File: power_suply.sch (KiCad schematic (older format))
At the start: 25 parts

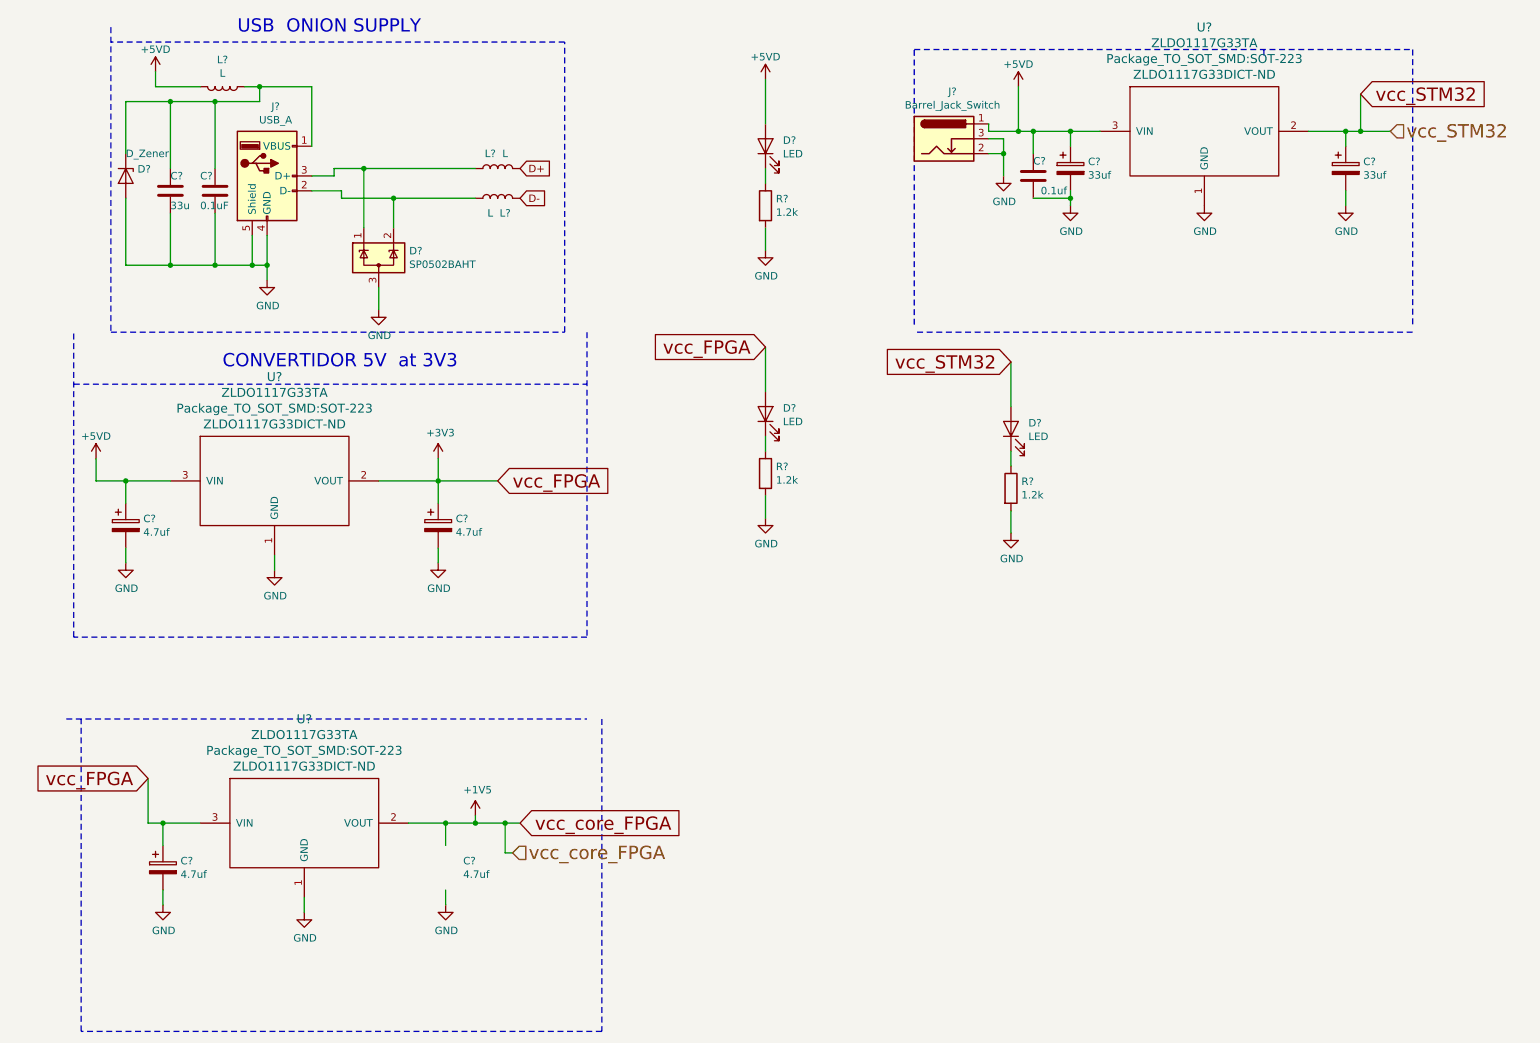
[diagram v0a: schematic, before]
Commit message: asignacion pines de control
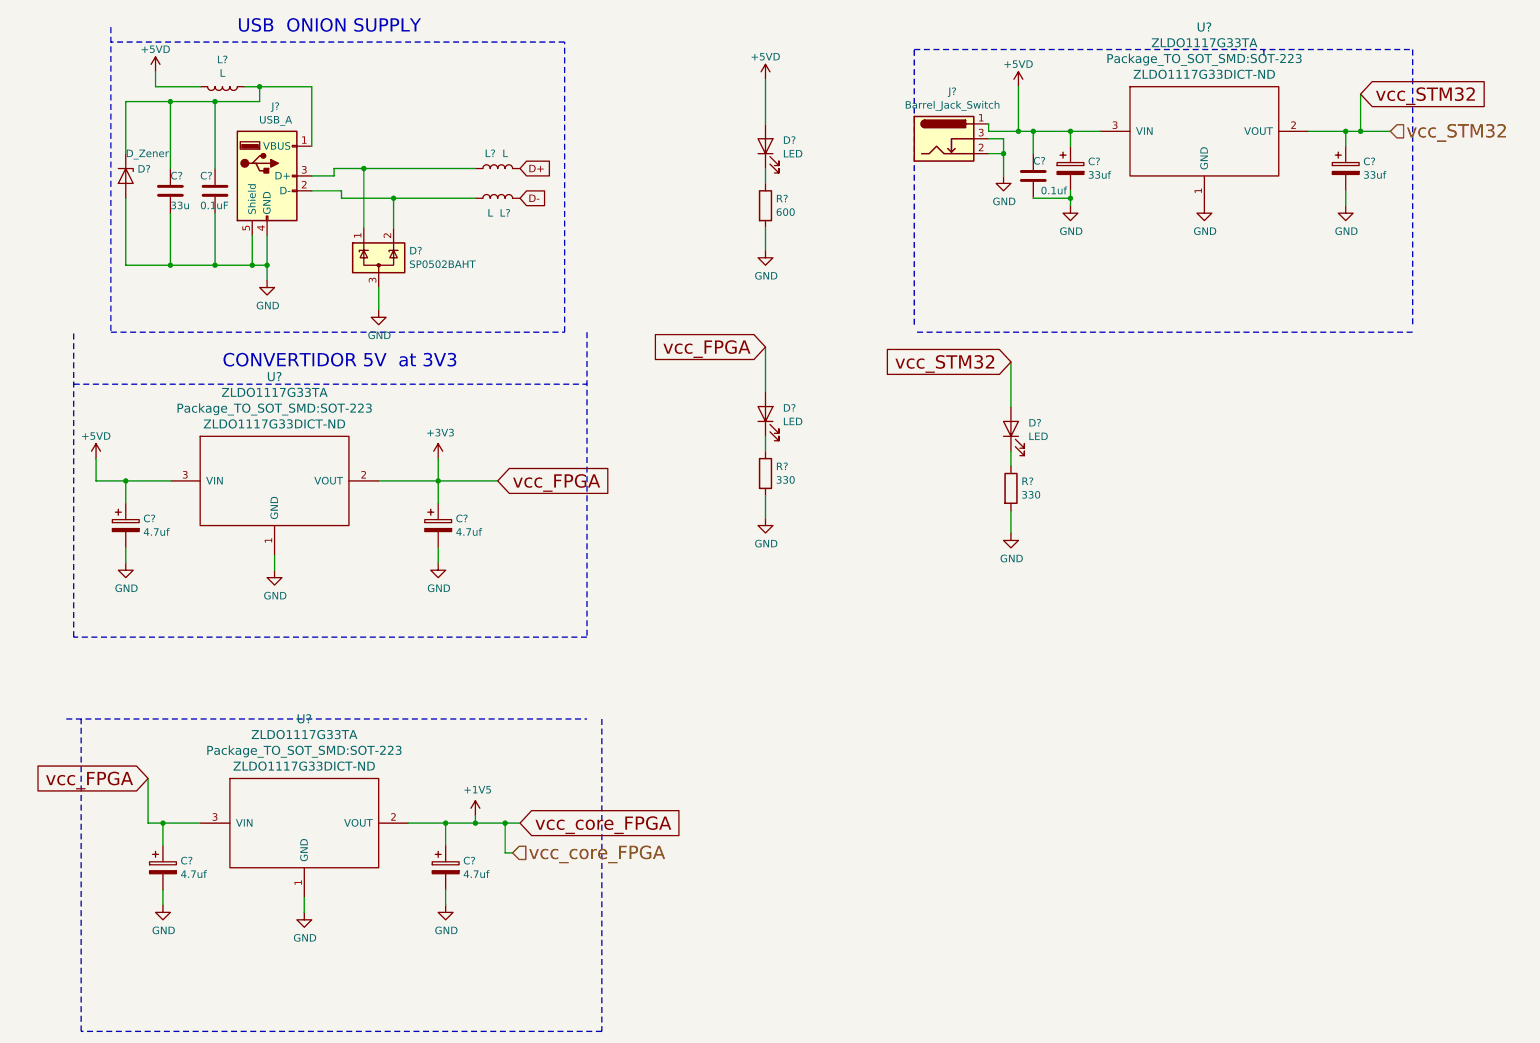
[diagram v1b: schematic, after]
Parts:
- removed D? (x2): LED, symbol BAT2032:LED
- added D? (x2): LED, LED_SMD:LED_0603_1608Metric, symbol BAT2032:LED
- D?: footprint (none) -> LED_SMD:LED_0603_1608Metric; digikey (none) -> 160-1436-1-ND rojo
- R?: value 1.2k -> 600
- R? (x2): value 1.2k -> 330
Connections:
- net +1V5: now also C?.1
- net +3V3: now also D?.2 (A)
- net GND: now also C?.2
- net vcc_STM32: now also D?.2 (A)
- net at R?.1: now also D?.1 (K) (x2)
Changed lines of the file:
@@
 $Descr A4 11693 8268
 encoding utf-8
-Sheet 2 5
+Sheet 2 6
 Title ""
 Date ""
@@
 $Comp
 L Device:CP C?
-U 0 0 5CD685F9
+U 1 1 5CD685F9
 P 3800 6500
 F 0 "C?" H 3918 6546 50  0000 L CNN
@@
 F 2 "" H 3838 6350 50  0001 C CNN
 F 3 "~" H 3800 6500 50  0001 C CNN
-	0    3800 6500
+	1    3800 6500
 	1    0    0    -1
 $EndComp
@@
 F 0 "D?" V 5989 1533 50  0000 R CNN
 F 1 "LED" V 5898 1533 50  0000 R CNN
-F 2 "" H 5950 1650 50  0001 C CNN
-F 3 "~" H 5950 1650 50  0001 C CNN
+F 2 "LED_SMD:LED_0603_1608Metric" H 5950 1650 50  0001 C CNN
+F 3 "http://optoelectronics.liteon.com/upload/download/DS-22-99-0151/LTST-C190KRKT.pdf" H 5950 1650 50  0001 C CNN
+F 4 "160-1436-1-ND     rojo" V 5950 1650 50  0001 C CNN "digikey"
 	1    5950 1650
 	0    -1   -1   0
@@
 P 5950 2050
 F 0 "R?" H 6020 2096 50  0000 L CNN
-F 1 "1.2k" H 6020 2005 50  0000 L CNN
+F 1 "600" H 6020 2005 50  0000 L CNN
 F 2 "Resistor_SMD:R_0603_1608Metric_Pad1.05x0.95mm_HandSolder" V 5880 2050 50  0001 C CNN
 F 3 "~" H 5950 2050 50  0001 C CNN
+F 4 "" H 5950 2050 50  0001 C CNN "Digikey"
 	1    5950 2050
 	1    0    0    -1
@@
 	5950 3000 5950 3300
 $Comp
-L BAT2032:LED D?
-U 1 1 5D5F584F
-P 5950 3450
-F 0 "D?" V 5989 3333 50  0000 R CNN
-F 1 "LED" V 5898 3333 50  0000 R CNN
-F 2 "" H 5950 3450 50  0001 C CNN
-F 3 "~" H 5950 3450 50  0001 C CNN
-	1    5950 3450
-	0    -1   -1   0
-$EndComp
-$Comp
 L BAT2032:R R?
 U 1 1 5D5F5855
 P 5950 3850
 F 0 "R?" H 6020 3896 50  0000 L CNN
-F 1 "1.2k" H 6020 3805 50  0000 L CNN
+F 1 "330" H 6020 3805 50  0000 L CNN
 F 2 "Resistor_SMD:R_0603_1608Metric_Pad1.05x0.95mm_HandSolder" V 5880 3850 50  0001 C CNN
 F 3 "~" H 5950 3850 50  0001 C CNN
@@
 	7600 3100 7600 3400
 $Comp
-L BAT2032:LED D?
-U 1 1 5D60A5BF
-P 7600 3550
-F 0 "D?" V 7639 3433 50  0000 R CNN
-F 1 "LED" V 7548 3433 50  0000 R CNN
-F 2 "" H 7600 3550 50  0001 C CNN
-F 3 "~" H 7600 3550 50  0001 C CNN
-	1    7600 3550
-	0    -1   -1   0
-$EndComp
-$Comp
 L BAT2032:R R?
 U 1 1 5D60A5C5
 P 7600 3950
 F 0 "R?" H 7670 3996 50  0000 L CNN
-F 1 "1.2k" H 7670 3905 50  0000 L CNN
+F 1 "330" H 7670 3905 50  0000 L CNN
 F 2 "Resistor_SMD:R_0603_1608Metric_Pad1.05x0.95mm_HandSolder" V 7530 3950 50  0001 C CNN
 F 3 "~" H 7600 3950 50  0001 C CNN
@@
 Text GLabel 7600 3100 0    89   Input ~ 0
 vcc_STM32
+$Comp
+L BAT2032:LED D?
+U 1 1 5D364419
+P 5950 3450
+F 0 "D?" V 5989 3333 50  0000 R CNN
+F 1 "LED" V 5898 3333 50  0000 R CNN
+F 2 "LED_SMD:LED_0603_1608Metric" H 5950 3450 50  0001 C CNN
+F 3 "~https://www.rohm.com/datasheet/SML-D12U1W" H 5950 3450 50  0001 C CNN
+F 4 "	846-1176-1-ND  Verde" V 5950 3450 50  0001 C CNN "digikey"
+	1    5950 3450
+	0    -1   -1   0
+$EndComp
+$Comp
+L BAT2032:LED D?
+U 1 1 5D366F3A
+P 7600 3550
+F 0 "D?" V 7639 3433 50  0000 R CNN
+F 1 "LED" V 7548 3433 50  0000 R CNN
+F 2 "LED_SMD:LED_0603_1608Metric" H 7600 3550 50  0001 C CNN
+F 3 "http://optoelectronics.liteon.com/upload/download/DS22-2010-0025/LTST-C194TBKT.PDF" H 7600 3550 50  0001 C CNN
+F 4 "160-1837-1-ND azul" V 7600 3550 50  0001 C CNN "digikey"
+	1    7600 3550
+	0    -1   -1   0
+$EndComp
 $EndSCHEMATC

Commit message: asignacion pines de control
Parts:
- gave numbers to parts that had none: 25

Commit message: retoque casi finales
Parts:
- added R13: 100, Resistor_SMD:R_0603_1608Metric_Pad1.05x0.95mm_HandSolder, symbol BAT2032:R
- C2, C3, C6: footprint (none) -> Capacitor_SMD:C_0603_1608Metric_Pad1.05x0.95mm_HandSolder
- D3, D4, D5: footprint LED_SMD:LED_0603_1608Metric -> LED_SMD:LED_0603_1608Metric_Pad1.05x0.95mm_HandSolder
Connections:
- wire segments 89 -> 94
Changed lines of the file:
@@
 F 0 "C3" H 1950 2050 50  0000 L CNN
 F 1 "33u" H 1950 1850 50  0000 L CNN
-F 2 "" H 1988 1800 50  0001 C CNN
+F 2 "Capacitor_SMD:C_0603_1608Metric_Pad1.05x0.95mm_HandSolder" H 1988 1800 50  0001 C CNN
 F 3 "~" H 1950 1950 50  0001 C CNN
 	1    1950 1950
@@
 F 0 "C2" H 2018 6546 50  0000 L CNN
 F 1 "4.7uf" H 2018 6455 50  0000 L CNN
-F 2 "" H 1938 6350 50  0001 C CNN
+F 2 "Capacitor_SMD:C_0603_1608Metric_Pad1.05x0.95mm_HandSolder" H 1938 6350 50  0001 C CNN
 F 3 "~" H 1900 6500 50  0001 C CNN
 	1    1900 6500
@@
 F 0 "C6" H 3918 6546 50  0000 L CNN
 F 1 "4.7uf" H 3918 6455 50  0000 L CNN
-F 2 "" H 3838 6350 50  0001 C CNN
+F 2 "Capacitor_SMD:C_0603_1608Metric_Pad1.05x0.95mm_HandSolder" H 3838 6350 50  0001 C CNN
 F 3 "~" H 3800 6500 50  0001 C CNN
 	1    3800 6500
@@
 vcc_FPGA
 Wire Wire Line
-	2150 6200 1900 6200
-Wire Wire Line
 	1800 6200 1800 5900
 Wire Wire Line
@@
 	1    0    0    -1
 $EndComp
-Wire Wire Line
-	3550 6200 3800 6200
 Wire Wire Line
 	4000 6200 4000 6150
@@
 $Comp
 L pcb_embedded_systems-cache:ZLDO1117G33TA U1
-U 1 1 5CDB7BFB
+U 0 0 5CDB7BFB
 P 2650 3900
 F 0 "U1" H 2650 4599 60  0000 C CNN
 F 1 "ZLDO1117G33TA" H 2650 4493 60  0000 C CNN
-F 2 "Package_TO_SOT_SMD:SOT-223" H 2650 4387 60  0000 C CNN
-F 3 "ZLDO1117G33DICT-ND" H 2650 4281 60  0000 C CNN
+F 2 "Package_TO_SOT_SMD:SOT-223" H 2650 4387 60  0001 C CNN
+F 3 "ZLDO1117G33DICT-ND" H 2650 4281 60  0001 C CNN
 F 4 "https://www.diodes.com/assets/Datasheets/ZLDO1117.pdf" H 2650 3900 50  0001 C CNN "digikey"
-	1    2650 3900
+	0    2650 3900
 	1    0    0    -1
 $EndComp
 $Comp
 L pcb_embedded_systems-cache:ZLDO1117G33TA U2
-U 1 1 5CE0B1BC
+U 0 0 5CE0B1BC
 P 2850 6200
 F 0 "U2" H 2850 6899 60  0000 C CNN
 F 1 "ZLDO1117G33TA" H 2850 6793 60  0000 C CNN
-F 2 "Package_TO_SOT_SMD:SOT-223" H 2850 6687 60  0000 C CNN
-F 3 "ZLDO1117G33DICT-ND" H 2850 6581 60  0000 C CNN
+F 2 "Package_TO_SOT_SMD:SOT-223" H 2850 6687 60  0001 C CNN
+F 3 "ZLDO1117G33DICT-ND" H 2850 6581 60  0001 C CNN
 F 4 "https://www.diodes.com/assets/Datasheets/ZLDO1117.pdf" H 2850 6200 50  0001 C CNN "digikey"
-	1    2850 6200
+	0    2850 6200
 	1    0    0    -1
 $EndComp
 $Comp
 L pcb_embedded_systems-cache:ZLDO1117G33TA U3
-U 1 1 5CE35DA7
+U 0 0 5CE35DA7
 P 8900 1550
 F 0 "U3" H 8900 2249 60  0000 C CNN
 F 1 "ZLDO1117G33TA" H 8900 2143 60  0000 C CNN
-F 2 "Package_TO_SOT_SMD:SOT-223" H 8900 2037 60  0000 C CNN
-F 3 "ZLDO1117G33DICT-ND" H 8900 1931 60  0000 C CNN
+F 2 "Package_TO_SOT_SMD:SOT-223" H 8900 2037 60  0001 C CNN
+F 3 "ZLDO1117G33DICT-ND" H 8900 1931 60  0001 C CNN
 F 4 "https://www.diodes.com/assets/Datasheets/ZLDO1117.pdf" H 8900 1550 50  0001 C CNN "digikey"
-	1    8900 1550
+	0    8900 1550
 	1    0    0    -1
 $EndComp
@@
 F 0 "D3" V 5989 1533 50  0000 R CNN
 F 1 "LED" V 5898 1533 50  0000 R CNN
-F 2 "LED_SMD:LED_0603_1608Metric" H 5950 1650 50  0001 C CNN
+F 2 "LED_SMD:LED_0603_1608Metric_Pad1.05x0.95mm_HandSolder" H 5950 1650 50  0001 C CNN
 F 3 "http://optoelectronics.liteon.com/upload/download/DS-22-99-0151/LTST-C190KRKT.pdf" H 5950 1650 50  0001 C CNN
 F 4 "160-1436-1-ND     rojo" V 5950 1650 50  0001 C CNN "digikey"
@@
 F 0 "D4" V 5989 3333 50  0000 R CNN
 F 1 "LED" V 5898 3333 50  0000 R CNN
-F 2 "LED_SMD:LED_0603_1608Metric" H 5950 3450 50  0001 C CNN
+F 2 "LED_SMD:LED_0603_1608Metric_Pad1.05x0.95mm_HandSolder" H 5950 3450 50  0001 C CNN
 F 3 "~https://www.rohm.com/datasheet/SML-D12U1W" H 5950 3450 50  0001 C CNN
 F 4 "	846-1176-1-ND  Verde" V 5950 3450 50  0001 C CNN "digikey"
@@
 F 0 "D5" V 7639 3433 50  0000 R CNN
 F 1 "LED" V 7548 3433 50  0000 R CNN
-F 2 "LED_SMD:LED_0603_1608Metric" H 7600 3550 50  0001 C CNN
+F 2 "LED_SMD:LED_0603_1608Metric_Pad1.05x0.95mm_HandSolder" H 7600 3550 50  0001 C CNN
 F 3 "http://optoelectronics.liteon.com/upload/download/DS22-2010-0025/LTST-C194TBKT.PDF" H 7600 3550 50  0001 C CNN
 F 4 "160-1837-1-ND azul" V 7600 3550 50  0001 C CNN "digikey"
@@
 	0    -1   -1   0
 $EndComp
+$Comp
+L BAT2032:R R13
+U 1 1 5DF0C6DE
+P 2850 7250
+F 0 "R13" V 2750 7250 50  0000 C CNN
+F 1 "100" V 2850 7250 50  0000 C CNN
+F 2 "Resistor_SMD:R_0603_1608Metric_Pad1.05x0.95mm_HandSolder" V 2780 7250 50  0001 C CNN
+F 3 "~" H 2850 7250 50  0001 C CNN
+	1    2850 7250
+	0    1    1    0
+$EndComp
+Wire Wire Line
+	2150 6200 1900 6200
+Wire Wire Line
+	3550 6200 3600 6200
+Wire Wire Line
+	3000 7250 3600 7250
+Wire Wire Line
+	3600 7250 3600 6200
+Connection ~ 3600 6200
+Wire Wire Line
+	3600 6200 3800 6200
+Wire Wire Line
+	2700 7250 2150 7250
+Wire Wire Line
+	2150 7250 2150 6200
+Connection ~ 2150 6200
 $EndSCHEMATC

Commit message: diseño de esquematico
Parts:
- removed C1, C5: 4.7uf, Capacitor_SMD:C_1206_3216Metric_Pad1.42x1.75mm_HandSolder, symbol Device:CP
- removed C2, C6: 4.7uf, Capacitor_SMD:C_0603_1608Metric_Pad1.05x0.95mm_HandSolder, symbol Device:CP
- removed C8, C9: 33uf, Capacitor_SMD:C_1206_3216Metric_Pad1.42x1.75mm_HandSolder, symbol Device:CP
- removed L2, L3: L, Inductor_SMD:L_0603_1608Metric_Pad1.05x0.95mm_HandSolder, symbol BAT2032:L
- added C1, C11, C2, C6, C8: 22uF, Capacitor_SMD:C_0603_1608Metric_Pad1.05x0.95mm_HandSolder, symbol Device:C
- added C10, C5, C7: 100nF, Capacitor_SMD:C_0603_1608Metric_Pad1.05x0.95mm_HandSolder, symbol Device:C
- added L2: SRF2012-900YA, library:SRF2012-900YA, symbol UL_SRF2012900YA:SRF2012-900YA
- C3: value 33u -> 22uF
- C9: renamed from C7; value 0.1uf -> 22uF
- D1: footprint (none) -> Diode_SMD:D_SOD-123; digikey (none) -> MMSZ5231BT1GOSCT-ND
- J2: footprint Connector_BarrelJack:BarrelJack_Horizontal -> PJ-002A:CUI_PJ-002A
- L1: digikey (none) -> 732-1593-1-ND
- renumbered R13 to R1, R1 to R2, R2 to R3, R3 to R4
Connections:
- net labels added: VCC_5V
- wire segments 94 -> 93
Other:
- note added: "DNP\n"

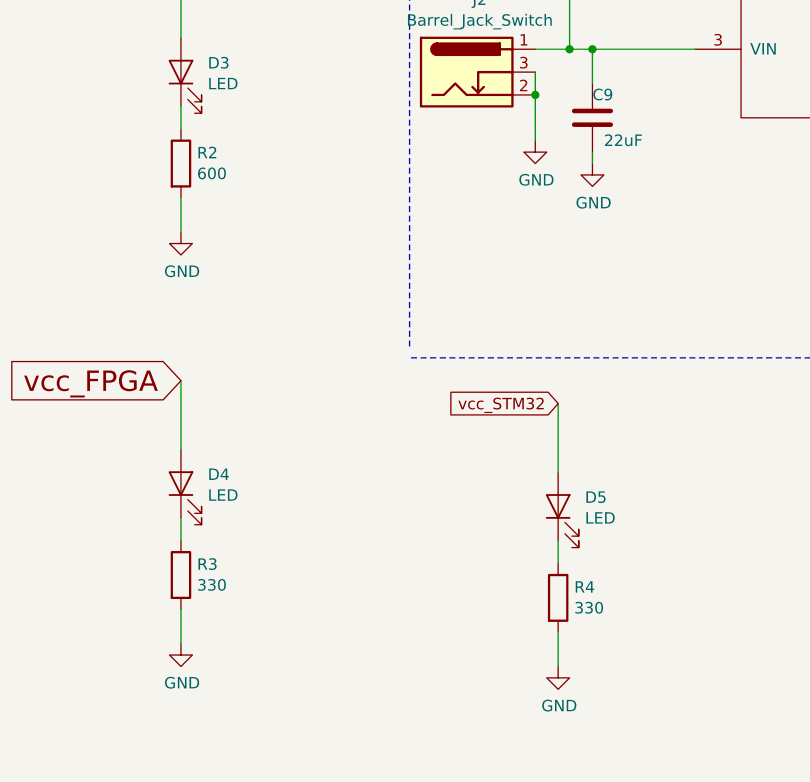
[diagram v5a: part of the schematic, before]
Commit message: programacion luego del diseño del embebido
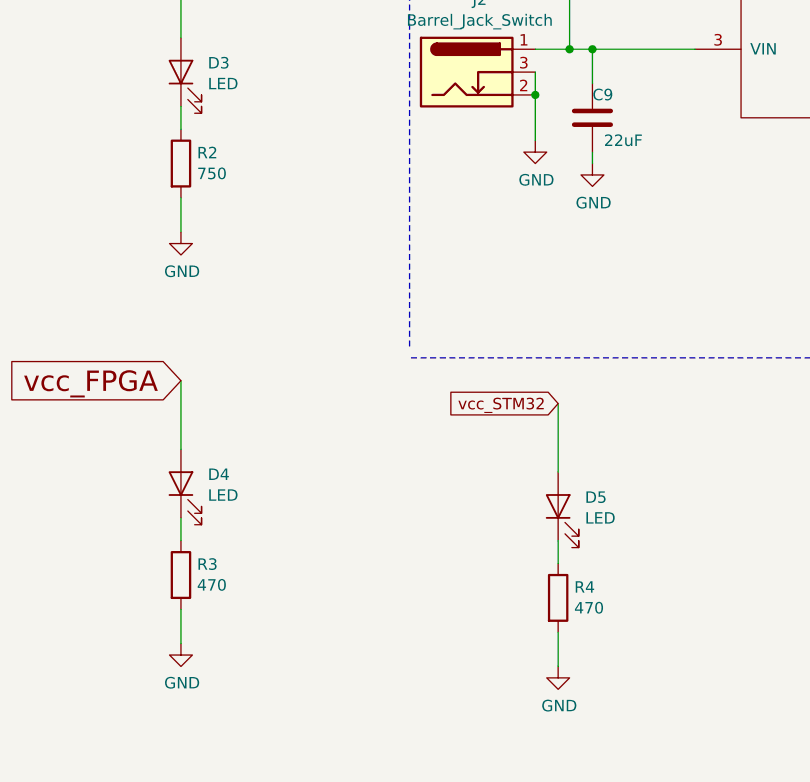
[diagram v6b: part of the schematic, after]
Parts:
- R2: value 600 -> 750
- R3, R4: value 330 -> 470
- U1, U2, U3: footprint Package_TO_SOT_SMD:SOT-223 -> Package_TO_SOT_SMD:SOT-223-3_TabPin2
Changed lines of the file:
@@
 F 0 "U1" H 2650 4599 60  0000 C CNN
 F 1 "ZLDO1117G33TA" H 2650 4493 60  0000 C CNN
-F 2 "Package_TO_SOT_SMD:SOT-223" H 2650 4387 60  0001 C CNN
+F 2 "Package_TO_SOT_SMD:SOT-223-3_TabPin2" H 2650 4387 60  0001 C CNN
 F 3 "ZLDO1117G33DICT-ND" H 2650 4281 60  0001 C CNN
 F 4 "https://www.diodes.com/assets/Datasheets/ZLDO1117.pdf" H 2650 3900 50  0001 C CNN "digikey"
@@
 F 0 "U2" H 2850 6899 60  0000 C CNN
 F 1 "ZLDO1117G33TA" H 2850 6793 60  0000 C CNN
-F 2 "Package_TO_SOT_SMD:SOT-223" H 2850 6687 60  0001 C CNN
+F 2 "Package_TO_SOT_SMD:SOT-223-3_TabPin2" H 2850 6687 60  0001 C CNN
 F 3 "ZLDO1117G33DICT-ND" H 2850 6581 60  0001 C CNN
 F 4 "https://www.diodes.com/assets/Datasheets/ZLDO1117.pdf" H 2850 6200 50  0001 C CNN "digikey"
@@
 F 0 "U3" H 8900 2249 60  0000 C CNN
 F 1 "ZLDO1117G33TA" H 8900 2143 60  0000 C CNN
-F 2 "Package_TO_SOT_SMD:SOT-223" H 8900 2037 60  0001 C CNN
+F 2 "Package_TO_SOT_SMD:SOT-223-3_TabPin2" H 8900 2037 60  0001 C CNN
 F 3 "ZLDO1117G33DICT-ND" H 8900 1931 60  0001 C CNN
 F 4 "https://www.diodes.com/assets/Datasheets/ZLDO1117.pdf" H 8900 1550 50  0001 C CNN "digikey"
@@
 P 5950 2050
 F 0 "R2" H 6020 2096 50  0000 L CNN
-F 1 "600" H 6020 2005 50  0000 L CNN
+F 1 "750" H 6020 2005 50  0000 L CNN
 F 2 "Resistor_SMD:R_0603_1608Metric_Pad1.05x0.95mm_HandSolder" V 5880 2050 50  0001 C CNN
 F 3 "~" H 5950 2050 50  0001 C CNN
-F 4 "" H 5950 2050 50  0001 C CNN "Digikey"
 	1    5950 2050
 	1    0    0    -1
@@
 P 5950 3850
 F 0 "R3" H 6020 3896 50  0000 L CNN
-F 1 "330" H 6020 3805 50  0000 L CNN
+F 1 "470" H 6020 3805 50  0000 L CNN
 F 2 "Resistor_SMD:R_0603_1608Metric_Pad1.05x0.95mm_HandSolder" V 5880 3850 50  0001 C CNN
 F 3 "~" H 5950 3850 50  0001 C CNN
@@
 P 7600 3950
 F 0 "R4" H 7670 3996 50  0000 L CNN
-F 1 "330" H 7670 3905 50  0000 L CNN
+F 1 "470" H 7670 3905 50  0000 L CNN
 F 2 "Resistor_SMD:R_0603_1608Metric_Pad1.05x0.95mm_HandSolder" V 7530 3950 50  0001 C CNN
 F 3 "~" H 7600 3950 50  0001 C CNN
